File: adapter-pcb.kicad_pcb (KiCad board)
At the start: 2 copper layers, 90.2 x 95.9 mm, 47 parts, among them J1 SS5-80-3.50-L-D-K-TR, J2 DM3BT-DSF-PEJS, J3 Conn_02x05_Odd_Even, Q1 2N7002KQ-7, Q2 2N7002KQ-7, U1 TXS0102QDCURQ1, U2 LTC4300A-1IMS8_PBF, U3 TXS02612RTWR, U4 TPS79933QDDCRQ1

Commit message: Made very tiny tweaks again
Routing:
- net /CSKB/I2C_SDA_CSKB: track 70.1 -> 73.7 mm, vias 2 -> 0
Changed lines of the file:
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@@
 			)
 		)
-		(property "MANUFACTURER" "  Texas Instruments"
+		(property "MANUFACTURER" "Texas Instruments"
 			(at 0 0 0)
 			(unlocked yes)
@@
 		(embedded_fonts no)
 		(model "${KICAD9_3DMODEL_DIR}/Connector_PinSocket_2.54mm.3dshapes/PinSocket_2x05_P2.54mm_Vertical.step"
+			(hide yes)
 			(offset
 				(xyz 0 0 0)
@@
 	)
 	(segment
-		(start 126.485662 94.846221)
-		(end 125.070661 96.261222)
+		(start 137.508778 107.141222)
+		(end 138.37585 106.27415)
 		(width 0.1524)
 		(layer "F.Cu")
@@
 	)
 	(segment
-		(start 125.070661 105.211222)
-		(end 127.000661 107.141222)
+		(start 127.787061 94.846221)
+		(end 126.485662 94.846221)
 		(width 0.1524)
 		(layer "F.Cu")
@@
 	)
 	(segment
-		(start 137.508778 107.141222)
-		(end 138.37585 106.27415)
+		(start 138.37585 106.27415)
+		(end 138.37585 103.726222)
 		(width 0.1524)
 		(layer "F.Cu")
@@
 	)
 	(segment
-		(start 127.000661 107.141222)
-		(end 137.508778 107.141222)
+		(start 126.485662 94.846221)
+		(end 124.91 96.421883)
 		(width 0.1524)
 		(layer "F.Cu")
@@
 	)
 	(segment
-		(start 125.070661 96.261222)
-		(end 125.070661 105.211222)
+		(start 124.91 105.050561)
+		(end 127.000661 107.141222)
 		(width 0.1524)
 		(layer "F.Cu")
@@
 	)
 	(segment
-		(start 127.787061 94.846221)
-		(end 126.485662 94.846221)
+		(start 124.91 96.421883)
+		(end 124.91 105.050561)
 		(width 0.1524)
 		(layer "F.Cu")
@@
 	)
 	(segment
-		(start 138.37585 106.27415)
-		(end 138.37585 103.726222)
+		(start 127.000661 107.141222)
+		(end 137.508778 107.141222)
 		(width 0.1524)
 		(layer "F.Cu")
@@
 	)
 	(segment
-		(start 182.55 114.95)
-		(end 179.97 114.95)
+		(start 170.18 59.2)
+		(end 171.49 57.89)
 		(width 0.254)
 		(layer "F.Cu")
@@
 	)
 	(segment
+		(start 171.49 57.89)
+		(end 173.31 57.89)
+		(width 0.254)
+		(layer "F.Cu")
+		(net "/CSKB/I2C_SDA_CSKB")
+	)
+	(segment
+		(start 174.01 58.59)
+		(end 174.01 66.79)
+		(width 0.254)
+		(layer "F.Cu")
+		(net "/CSKB/I2C_SDA_CSKB")
+	)
+	(segment
+		(start 174.01 66.79)
+		(end 184.52 77.3)
+		(width 0.254)
+		(layer "F.Cu")
+		(net "/CSKB/I2C_SDA_CSKB")
+	)
+	(segment
 		(start 179.8 119.49)
 		(end 179.8 118.79)
@@
 	)
 	(segment
-		(start 179.515 115.405)
-		(end 179.515 116.8898)
+		(start 182.55 114.95)
+		(end 179.97 114.95)
 		(width 0.254)
 		(layer "F.Cu")
@@
 	)
 	(segment
-		(start 184.52 112.98)
-		(end 182.55 114.95)
+		(start 173.31 57.89)
+		(end 174.01 58.59)
 		(width 0.254)
 		(layer "F.Cu")
@@
 	)
 	(segment
-		(start 170.18 62.96)
-		(end 170.18 59.2)
+		(start 179.515 115.405)
+		(end 179.515 116.8898)
 		(width 0.254)
 		(layer "F.Cu")
@@
 	)
 	(segment
-		(start 174.18 66.96)
-		(end 184.52 77.3)
+		(start 184.52 112.98)
+		(end 182.55 114.95)
 		(width 0.254)
 		(layer "F.Cu")
 		(net "/CSKB/I2C_SDA_CSKB")
 	)
-	(via
-		(at 170.18 62.96)
-		(size 0.61)
-		(drill 0.3)
-		(layers "F.Cu" "B.Cu")
-		(net "/CSKB/I2C_SDA_CSKB")
-	)
-	(via
-		(at 174.18 66.96)
-		(size 0.61)
-		(drill 0.3)
-		(layers "F.Cu" "B.Cu")
-		(net "/CSKB/I2C_SDA_CSKB")
-	)
-	(segment
-		(start 170.18 62.96)
-		(end 174.18 66.96)
-		(width 0.254)
-		(layer "B.Cu")
-		(net "/CSKB/I2C_SDA_CSKB")
-	)
 	(segment
-		(start 179.515 113.985)
-		(end 179.82 114.29)
+		(start 179.515 112.4702)
+		(end 179.515 113.985)
 		(width 0.254)
 		(layer "F.Cu")
@@
 	)
 	(segment
-		(start 172.72 68.36)
-		(end 172.72 59.2)
+		(start 183.21 77.89)
+		(end 172.72 67.4)
 		(width 0.254)
 		(layer "F.Cu")
@@
 	)
 	(segment
-		(start 182 114.29)
-		(end 183.06 113.23)
-		(width 0.254)
+		(start 179.41 112.3652)
+		(end 179.515 112.4702)
+		(width 0.2)
 		(layer "F.Cu")
 		(net "/CSKB/I2C_SCL_CSKB")
 	)
 	(segment
-		(start 179.515 112.4702)
-		(end 179.515 113.985)
+		(start 172.72 67.4)
+		(end 172.72 59.2)
 		(width 0.254)
 		(layer "F.Cu")
@@
 	)
 	(segment
-		(start 179.41 112.3652)
-		(end 179.515 112.4702)
+		(start 179.515 110.065)
+		(end 179.41 109.96)
 		(width 0.2)
 		(layer "F.Cu")
@@
 	)
 	(segment
-		(start 179.515 110.065)
-		(end 179.41 109.96)
-		(width 0.2)
+		(start 179.515 113.985)
+		(end 179.82 114.29)
+		(width 0.254)
 		(layer "F.Cu")
 		(net "/CSKB/I2C_SCL_CSKB")
@@
 	)
 	(segment
-		(start 183.06 78.7)
-		(end 172.72 68.36)
+		(start 183.21 112.59)
+		(end 183.21 77.89)
 		(width 0.254)
 		(layer "F.Cu")
@@
 	)
 	(segment
-		(start 183.06 113.23)
-		(end 183.06 78.7)
+		(start 179.82 114.29)
+		(end 181.51 114.29)
 		(width 0.254)
 		(layer "F.Cu")
@@
 	)
 	(segment
-		(start 179.82 114.29)
-		(end 182 114.29)
+		(start 181.51 114.29)
+		(end 183.21 112.59)
 		(width 0.254)
 		(layer "F.Cu")
@@
 	)
 	(zone
-		(net "/CSKB/I2C_SCL_CSKB")
+		(net "/CSKB/I2C_SDA_CSKB")
 		(layer "F.Cu")
 		(hatch none 0.1)
@@
 		(polygon
 			(pts
-				(xy 172.847 60.846027) (xy 172.851896 60.695606) (xy 172.866172 60.568675) (xy 172.887142 60.468815)
-				(xy 172.915088 60.382293) (xy 172.991273 60.234389) (xy 173.127601 60.055449) (xy 173.278569 59.861761)
-				(xy 173.36128 59.73824) (xy 173.447585 59.588902) (xy 172.72 59.195027) (xy 171.992415 59.588902)
-				(xy 172.143445 59.836287) (xy 172.312399 60.055449) (xy 172.427066 60.202333) (xy 172.474957 60.27739)
-				(xy 172.515653 60.359429) (xy 172.548481 60.452882) (xy 172.572764 60.56218) (xy 172.587829 60.691751)
-				(xy 172.593 60.846027)
+				(xy 171.254114 57.946281) (xy 171.144288 58.049182) (xy 171.04444 58.128841) (xy 170.959 58.184625)
+				(xy 170.878059 58.226045) (xy 170.719605 58.276757) (xy 170.496677 58.306888) (xy 170.252969 58.337095)
+				(xy 170.107141 58.365952) (xy 169.940515 58.410524) (xy 170.176484 59.203516) (xy 170.969476 59.439485)
+				(xy 171.037609 59.157763) (xy 171.073111 58.883323) (xy 171.095892 58.698379) (xy 171.1151 58.611442)
+				(xy 171.144334 58.524654) (xy 171.187204 58.435361) (xy 171.247318 58.340905) (xy 171.328286 58.238632)
+				(xy 171.433719 58.125886)
 			)
 		)
@@
 	)
 	(zone
-		(net "/CSKB/I2C_SDA_CSKB")
+		(net "/CSKB/I2C_SCL_CSKB")
 		(layer "F.Cu")
 		(hatch none 0.1)
@@
 		(polygon
 			(pts
-				(xy 170.307 60.846027) (xy 170.311896 60.695606) (xy 170.326172 60.568675) (xy 170.347142 60.468815)
-				(xy 170.375088 60.382293) (xy 170.451273 60.234389) (xy 170.587601 60.055449) (xy 170.738569 59.861761)
-				(xy 170.82128 59.73824) (xy 170.907585 59.588902) (xy 170.18 59.195027) (xy 169.452415 59.588902)
-				(xy 169.603445 59.836287) (xy 169.772399 60.055449) (xy 169.887066 60.202333) (xy 169.934957 60.27739)
-				(xy 169.975653 60.359429) (xy 170.008481 60.452882) (xy 170.032764 60.56218) (xy 170.047829 60.691751)
-				(xy 170.053 60.846027)
+				(xy 172.847 60.846027) (xy 172.851896 60.695606) (xy 172.866172 60.568675) (xy 172.887142 60.468815)
+				(xy 172.915088 60.382293) (xy 172.991273 60.234389) (xy 173.127601 60.055449) (xy 173.278569 59.861761)
+				(xy 173.36128 59.73824) (xy 173.447585 59.588902) (xy 172.72 59.195027) (xy 171.992415 59.588902)
+				(xy 172.143445 59.836287) (xy 172.312399 60.055449) (xy 172.427066 60.202333) (xy 172.474957 60.27739)
+				(xy 172.515653 60.359429) (xy 172.548481 60.452882) (xy 172.572764 60.56218) (xy 172.587829 60.691751)
+				(xy 172.593 60.846027)
 			)
 		)

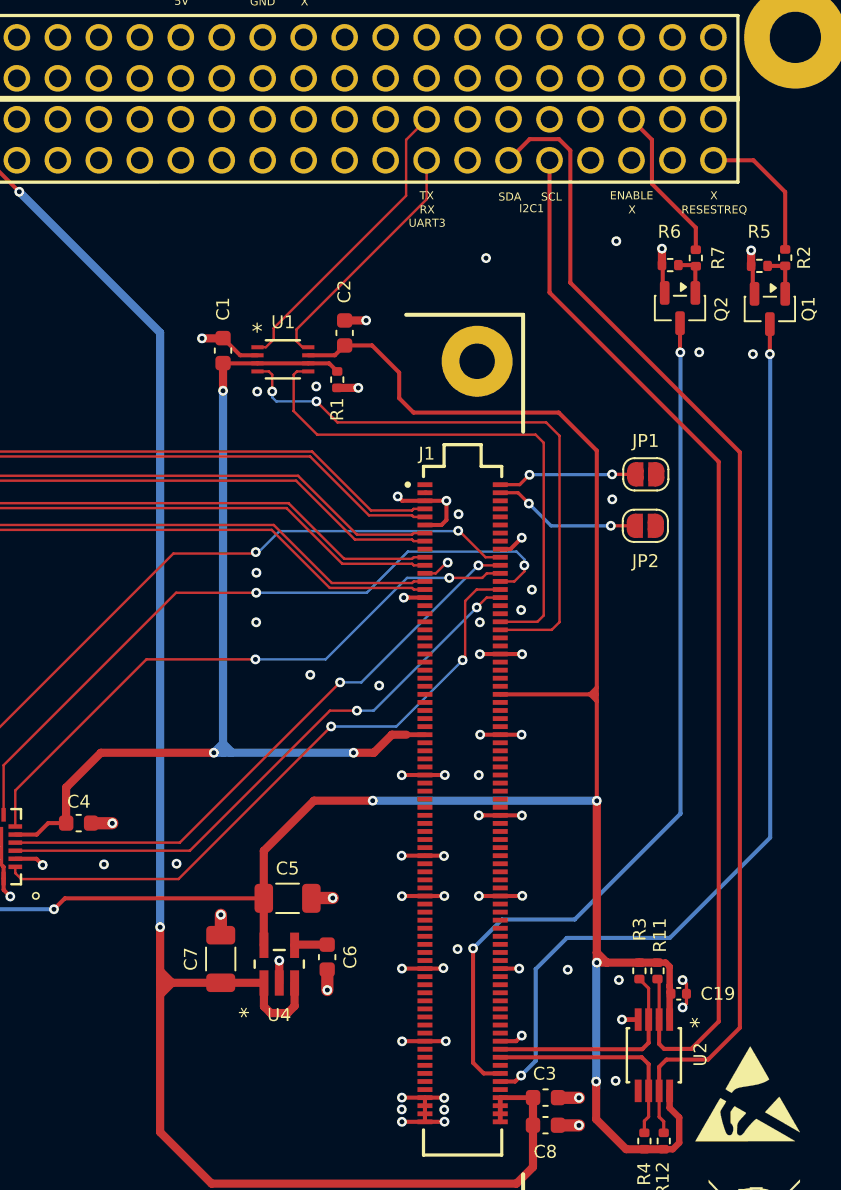
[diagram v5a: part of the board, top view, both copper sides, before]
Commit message: added solder bridges and updated BOM
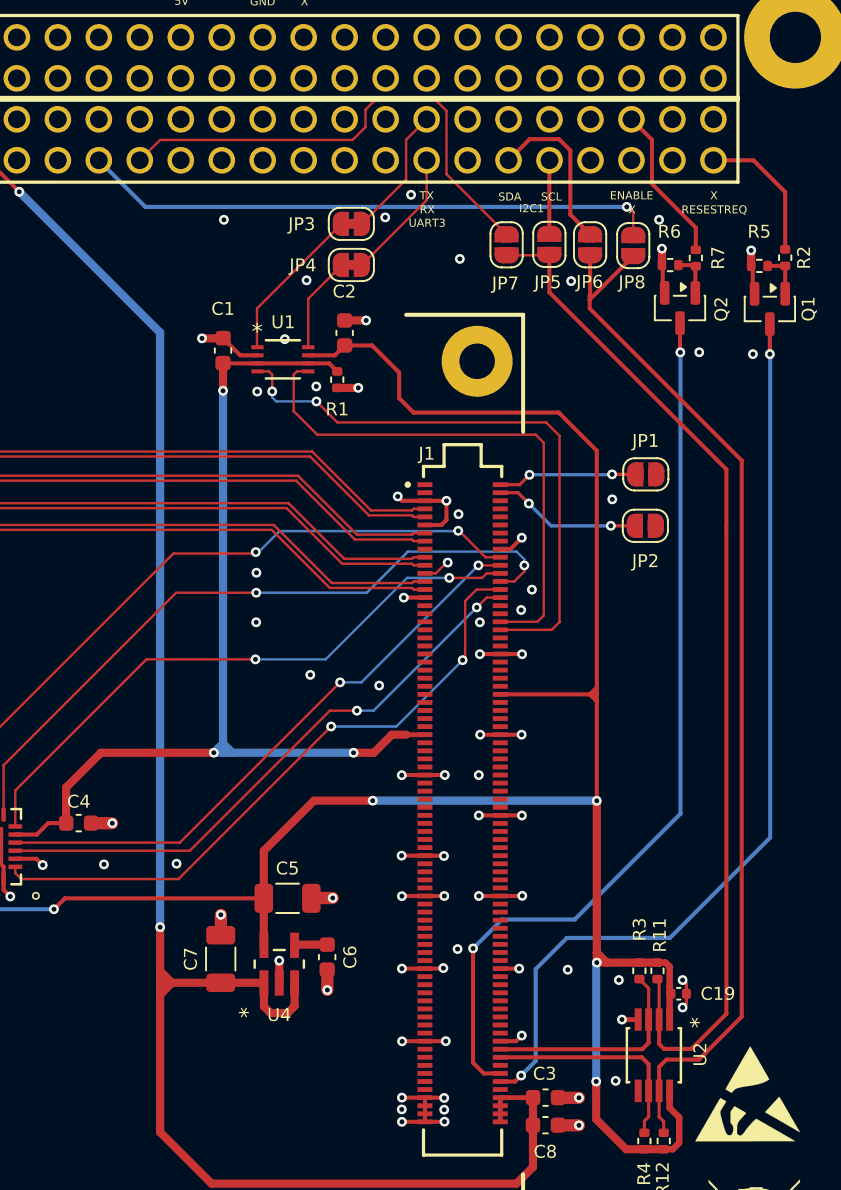
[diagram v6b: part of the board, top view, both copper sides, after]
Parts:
- added JP3: SolderJumper_2_Open, Jumper:SolderJumper-2_P1.3mm_Bridged_RoundedPad1.0x1.5mm, F.Cu at (160.4, 63.1)
- added JP4: SolderJumper_2_Open, Jumper:SolderJumper-2_P1.3mm_Bridged_RoundedPad1.0x1.5mm, F.Cu at (160.4, 65.7)
- added JP5: SolderJumper_2_Open, Jumper:SolderJumper-2_P1.3mm_Open_RoundedPad1.0x1.5mm, F.Cu at (172.7, 64.4)
- added JP6: SolderJumper_2_Open, Jumper:SolderJumper-2_P1.3mm_Open_RoundedPad1.0x1.5mm, F.Cu at (175.2, 64.4)
- added JP7: SolderJumper_2_Open, Jumper:SolderJumper-2_P1.3mm_Open_RoundedPad1.0x1.5mm, F.Cu at (170.1, 64.4)
- added JP8: SolderJumper_2_Open, Jumper:SolderJumper-2_P1.3mm_Open_RoundedPad1.0x1.5mm, F.Cu at (177.9, 64.5)
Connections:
- H1 pad 21: unconnected-(H1-Pin_21-Pad21) -> Net-(H1-Pin_21)
- H1 pad 23: unconnected-(H1-Pin_23-Pad23) -> Net-(H1-Pin_23)
- H1 pad 37: /CSKB/UART-RXD LS -> Net-(H1-Pin_37)
- H1 pad 38: /CSKB/UART-TXD LS -> Net-(H1-Pin_38)
- H1 pad 41: /CSKB/I2C_SDA_CSKB -> Net-(H1-Pin_41)
- H1 pad 43: /CSKB/I2C_SCL_CSKB -> Net-(H1-Pin_43)
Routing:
- net Net-(H1-Pin_21): track 0.00 -> 35.9 mm, vias 0 -> 1
- net Net-(H1-Pin_23): track 0.00 -> 30.8 mm
- net Net-(H1-Pin_41): track 0.00 -> 10.5 mm
- net /CSKB/UART-RXD LS: track 15.4 -> 6.00 mm
- net /CSKB/UART-TXD LS: track 19.2 -> 9.82 mm
- net Net-(H1-Pin_38): track 0.00 -> 8.54 mm
- net /CSKB/I2C_SDA_CSKB: track 73.7 -> 65.5 mm
- net Net-(H1-Pin_37): track 0.00 -> 8.15 mm
- net Net-(H1-Pin_43): track 0.00 -> 4.57 mm
- net /CSKB/I2C_SCL_CSKB: track 66.5 -> 63.7 mm
- net GND: vias 75 -> 81
